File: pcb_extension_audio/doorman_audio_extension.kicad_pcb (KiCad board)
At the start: 4 copper layers, 31.4 x 29.6 mm, 45 parts, among them J1 Audio Out, J2 GPIO, J4 Extension Board Connector, J5 Audio In, U1 ES8388

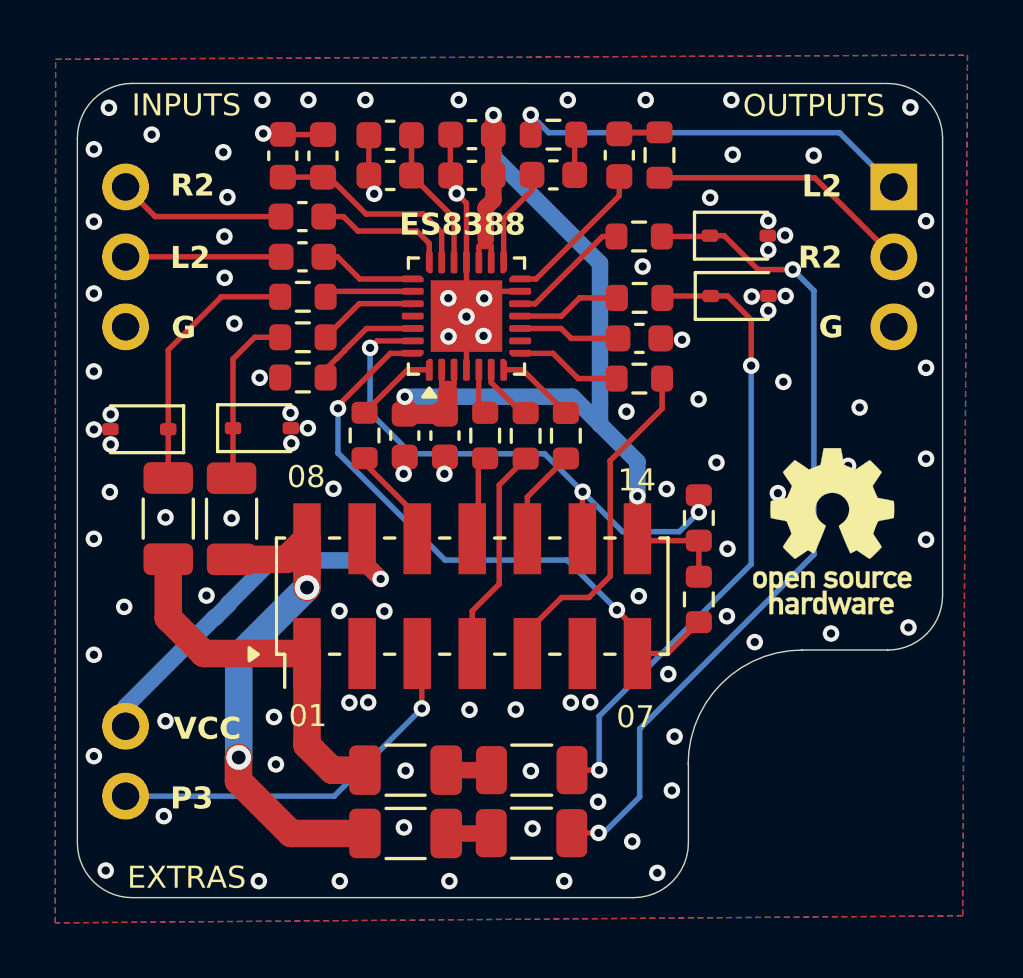
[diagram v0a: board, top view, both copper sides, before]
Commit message: WIP virtual devices
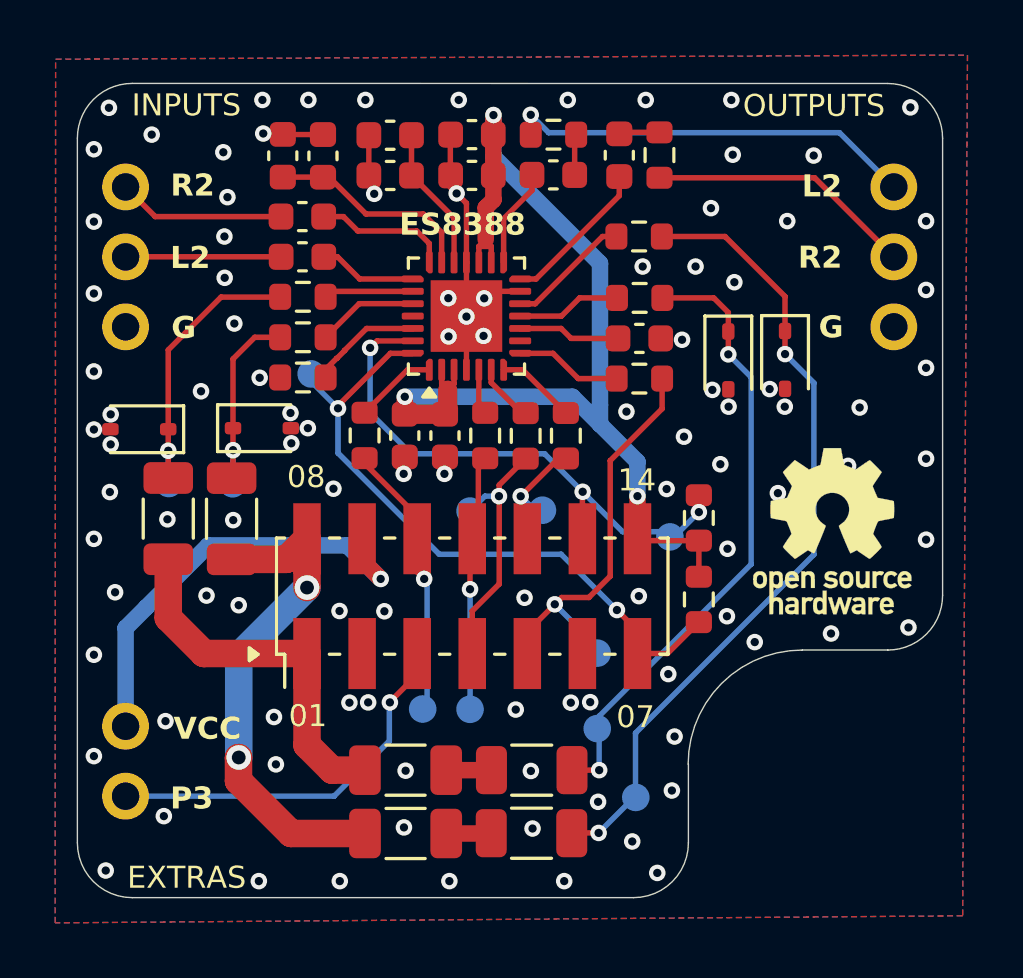
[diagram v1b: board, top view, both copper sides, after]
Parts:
- added TP1: Test Point IN L1, TestPoint:TestPoint_Pad_D1.0mm, B.Cu at (89.0, 62.4)
- added TP10: Test Point I2S DAT IN, TestPoint:TestPoint_Pad_D1.0mm, B.Cu at (97.6, 63.3)
- added TP11: Test Point I2S DAT OUT, TestPoint:TestPoint_Pad_D1.0mm, B.Cu at (102.2, 68.5)
- added TP2: Test Point IN R1, TestPoint:TestPoint_Pad_D1.0mm, B.Cu at (86.7, 62.3)
- added TP3: Test Point OUT L1, TestPoint:TestPoint_Pad_D1.0mm, B.Cu at (103.6, 73.7)
- added TP4: Test Point OUT R1, TestPoint:TestPoint_Pad_D1.0mm, B.Cu at (102.2, 71.2)
- added TP5: Test Point I2C CLK, TestPoint:TestPoint_Pad_D1.0mm, B.Cu at (91.8, 58.4)
- added TP6: Test Point I2C DAT, TestPoint:TestPoint_Pad_D1.0mm, B.Cu at (104.9, 64.3)
- added TP7: Test Point I2S MCLK, TestPoint:TestPoint_Pad_D1.0mm, B.Cu at (95.9, 70.5)
- added TP8: Test Point I2S BCLK, TestPoint:TestPoint_Pad_D1.0mm, B.Cu at (97.6, 70.5)
- added TP9: Test Point I2S LRCLK, TestPoint:TestPoint_Pad_D1.0mm, B.Cu at (100.2, 63.3)
- D1, D2, D3, D4: value CDSOD323-T03S -> TPCDSOD323-T03SC
- moved D2 4.81 mm to (109.0, 57.9), turned to -90 degrees
- moved D4 2.38 mm to (107.0, 57.9), turned to -90 degrees
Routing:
- net I2S_MCLK: track 4.13 -> 10.5 mm, vias 0 -> 1
- net I2S_BCLK: track 3.15 -> 9.38 mm, vias 0 -> 1
- net I2S_DAT_OUT: track 12.6 -> 15.0 mm, vias 0 -> 1
- net VCC: track 14.3 -> 16.4 mm
- net I2C_CLK: track 22.3 -> 24.0 mm
- net I2S_LRCK: track 3.49 -> 4.88 mm, vias 0 -> 1
- net I2S_DAT_IN: track 7.94 -> 9.22 mm, vias 0 -> 1
- net Net-(D1-K): track 6.39 -> 7.61 mm, vias 0 -> 1
- net Net-(D3-K): track 9.52 -> 10.7 mm, vias 0 -> 1
- net Net-(D2-K): track 30.4 -> 29.5 mm
- net PIN3: track 14.7 -> 14.0 mm
- net GND: vias 102 -> 104
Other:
- board text added: "08 BUS 09 VCC 10 I²S MCLK 11 I²S BCLK 12 I²S LRCK 13 I²C DAT 14 3V3"
- board text added: "BUS 01 GND 02 P3 03 I²S DIN 04 I²S DOUT 05 GND 06 I²C CLK 07"
- board text removed: "08 BUS 09 VCC 10 I²S BCLK 11 I²S DIN 12 I²S LRCK 13 I²C DAT 14 3V3"
- board text removed: "BUS 01 GND 02 I²S MCLK 03 P4 04 I²S DOUT 05 GND 06 I²C CLK 07"

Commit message: WIP
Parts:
- removed C13: 1uF, Capacitor_SMD:C_0603_1608Metric
- removed J5: Audio In, Connector_PinHeader_2.54mm:PinHeader_1x03_P2.54mm_Vertical
- removed R4, R7, R8, R9: 0, Resistor_SMD:R_0603_1608Metric
- removed U1: ES8388, Package_DFN_QFN:QFN-28-1EP_4x4mm_P0.45mm_EP2.6x2.6mm
- added C6: 1uF, Capacitor_SMD:C_0603_1608Metric, F.Cu at (89.3, 50.1)
- added J3: ~, Connector_PinHeader_2.54mm:PinHeader_1x03_P2.54mm_Vertical, F.Cu at (85.1, 55.7)
- added R1: 10K, Resistor_SMD:R_0603_1608Metric, F.Cu at (98.5, 49.3)
- added R11: 10K, Resistor_SMD:R_0603_1608Metric, F.Cu at (95.4, 50.8)
- added R12: 10K, Resistor_SMD:R_0603_1608Metric, F.Cu at (93.0, 52.3)
- added U2: ES8311, Doorman:QFN40P300X300X60-21N, F.Cu at (96.8, 55.6)
- J1: value Audio Out -> ~; moved to F.Cu
- R2, R3: value 10 -> 10K
- moved C5 17.6 mm to (108.6, 58.5), turned to 0 degrees
- moved C3 17.5 mm to (108.5, 56.6), turned to 0 degrees
- moved TP3 15.7 mm to (110.1, 59.5)
- moved TP7 14.4 mm to (91.7, 56.7)
- moved TP4 13.1 mm to (107.8, 59.4)
- moved C7 12.2 mm to (88.6, 53.1), turned to -90 degrees
- moved C20 11.9 mm to (102.7, 50.1)
- moved C2 11.2 mm to (100.3, 60.6), turned to 90 degrees
- moved C1 10.3 mm to (101.8, 60.6), turned to 90 degrees
- moved TP9 10.1 mm to (90.9, 59.4)
- moved R3 9.14 mm to (95.4, 49.4), turned to 0 degrees
- moved C21 9.03 mm to (101.3, 50.1)
- moved C19 8.36 mm to (102.0, 53.8), turned to 180 degrees
- moved R19 8.12 mm to (95.9, 60.6), turned to -90 degrees
- moved C18 7.39 mm to (102.0, 52.3), turned to 180 degrees
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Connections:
- net Net-(U1-ADCVREF) renamed ADCVREF
- net Net-(U1-VMID) renamed VMID
- C1 pad 2: +3.3V -> AVDD
- C10 pad 2: +3.3V -> AVDD
- C11 pad 2: +3.3V -> AVDD
- C12 pad 2: Net-(D3-K) -> AUDIO_IN_P
- C17 pad 2: Net-(U1-VREF) -> DACVREF
- C2 pad 2: +3.3V -> AVDD
- C3 pad 1: Net-(U1-RIN2) -> AUDIO_OUT_P
- C3 pad 2: AUDIO_IN_R2 -> Net-(J1-Pin_2)
- C4 pad 2: Net-(D1-K) -> AUDIO_IN_N
- C5 pad 1: Net-(U1-LIN2) -> AUDIO_OUT_N
- C5 pad 2: AUDIO_IN_L2 -> Net-(J1-Pin_1)
- C7 pad 1: Net-(U1-LOUT2) -> AUDIO_IN_N
- C7 pad 2: Net-(C7-Pad2) -> Net-(J3-Pin_1)
- D1 pad 1: Net-(D1-K) -> AUDIO_IN_N
- D2 pad 1: Net-(D2-K) -> AUDIO_OUT_P
- D3 pad 1: Net-(D3-K) -> AUDIO_IN_P
- D4 pad 1: Net-(D4-K) -> AUDIO_OUT_N
- J1 pad 1: AUDIO_OUT_L2 -> Net-(J1-Pin_1)
- J1 pad 2: AUDIO_OUT_R2 -> Net-(J1-Pin_2)
- J2 pad 1: PIN3 -> PIN2
- J2 pad 2: VCC -> GND
- J4 pad 11: I2S_BCLK -> I2S_LRCK
- J4 pad 12: I2S_LRCK -> I2S_DAT_IN
- J4 pad 14: +3.3V -> AVDD
- J4 pad 2: GND -> PIN2
- J4 pad 3: PIN3 -> GND
- J4 pad 4: I2S_DAT_IN -> I2S_BCLK
- J4 pad 9: VCC -> GND
- R10 pad 1: Net-(D2-K) -> AUDIO_OUT_P
- R13 pad 1: +3.3V -> AVDD
- R14 pad 1: +3.3V -> AVDD
- R2 pad 1: Net-(C7-Pad2) -> AUDIO_IN_N
- R2 pad 2: AUDIO_OUT_L2 -> GND
- R3 pad 1: Net-(C13-Pad2) -> AVDD
- R3 pad 2: AUDIO_OUT_R2 -> AUDIO_IN_P
- R5 pad 1: GND -> CE
- R5 pad 2: Net-(U1-CE) -> GND
- R6 pad 1: Net-(D4-K) -> AUDIO_OUT_N
- TP1 pad 1: Net-(D1-K) -> AUDIO_IN_N
- TP2 pad 1: Net-(D3-K) -> AUDIO_IN_P
- TP3 pad 1: Net-(D2-K) -> AUDIO_OUT_P
- TP4 pad 1: Net-(D4-K) -> AUDIO_OUT_N
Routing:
- net AVDD: track 0.00 -> 55.8 mm, vias 0 -> 5
- net +3.3V: track 40.3 -> 0.00 mm, vias 3 -> 0
- net AUDIO_OUT_P: track 0.00 -> 34.7 mm, vias 0 -> 2
- net Net-(D2-K): track 29.5 -> 0.00 mm, vias 2 -> 0
- net AUDIO_OUT_N: track 0.00 -> 29.2 mm, vias 0 -> 2
- net AUDIO_IN_P: track 0.00 -> 27.6 mm, vias 0 -> 3
- net AUDIO_IN_N: track 0.00 -> 26.8 mm, vias 0 -> 3
- net Net-(D4-K): track 22.9 -> 0.00 mm, vias 2 -> 0
- net PIN2: track 0.00 -> 17.0 mm, vias 0 -> 1
- net VCC: track 16.4 -> 0.00 mm, vias 1 -> 0
- net AUDIO_OUT_L2: track 15.0 -> 0.00 mm, vias 1 -> 0
- net PIN3: track 14.0 -> 0.00 mm, vias 1 -> 0
- net Net-(D3-K): track 10.7 -> 0.00 mm, vias 1 -> 0
- net AUDIO_OUT_R2: track 9.70 -> 0.00 mm
- net GND: track 14.0 -> 5.14 mm, vias 104 -> 92
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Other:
- board text added: "+"
- board text added: "-"
- board text added: "08 BUS 09 GND 10 I²S MCLK 11 I²S LRCK 12 I²S DIN 13 I²C DAT 14 3V3"
- board text added: "BUS 01 P2 02 GND 03 I²S BCLK 04 I²S DOUT 05 GND 06 I²C CLK 07"
- board text added: "ES8311"
- board text added: "GND"
- board text added: "GPIO"
- board text added: "INPUT"
- board text added: "OUTPUT"
- board text added: "P2"
- board text removed: "08 BUS 09 VCC 10 I²S MCLK 11 I²S BCLK 12 I²S LRCK 13 I²C DAT 14 3V3"
- board text removed: "BUS 01 GND 02 P3 03 I²S DIN 04 I²S DOUT 05 GND 06 I²C CLK 07"
- board text removed: "ES8388"
- board text removed: "EXTRAS"
- board text removed: "INPUTS"
- board text removed: "L2"
- board text removed: "OUTPUTS"
- board text removed: "P3"
- board text removed: "R2"
- board text removed: "VCC"

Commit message: WIP
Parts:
- added C13: 10uF, Capacitor_SMD:C_0402_1005Metric, F.Cu at (96.0, 51.8)
- added C9: 10uF, Capacitor_SMD:C_0402_1005Metric, F.Cu at (97.8, 51.8)
- J1: value ~ -> Output
- J3: value ~ -> Input
- moved TP5 16.6 mm to (104.7, 65.6)
- moved J1 2.93 mm to (113.0, 55.7)
- moved TP7 2.28 mm to (91.5, 54.5)
- moved C7 1.85 mm to (88.4, 54.9)
- moved C5 0.26 mm to (108.3, 58.4)
- moved C3 0.22 mm to (108.3, 56.6)
- moved R1 0.19 mm to (98.4, 49.2)
- moved R2 0.19 mm to (98.4, 50.6)
- moved R3 0.19 mm to (95.5, 49.2)
- moved R11 0.19 mm to (95.5, 50.6)
- moved C6 0.09 mm to (89.2, 50.1)
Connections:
- C12 pad 2: AUDIO_IN_P -> Net-(D3-K)
- C4 pad 2: AUDIO_IN_N -> Net-(D1-K)
- D1 pad 1: AUDIO_IN_N -> Net-(D1-K)
- D3 pad 1: AUDIO_IN_P -> Net-(D3-K)
- R1 pad 1: AVDD -> Net-(D1-K)
- R1 pad 2: AUDIO_IN_N -> Net-(C9-Pad2)
- R11 pad 1: AUDIO_IN_P -> Net-(C13-Pad2)
- R2 pad 1: AUDIO_IN_N -> Net-(C9-Pad2)
- R3 pad 1: AVDD -> Net-(D3-K)
- R3 pad 2: AUDIO_IN_P -> Net-(C13-Pad2)
- TP1 pad 1: AUDIO_IN_N -> Net-(D1-K)
- TP2 pad 1: AUDIO_IN_P -> Net-(D3-K)
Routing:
- net Net-(D1-K): track 0.00 -> 23.5 mm, vias 0 -> 2
- net Net-(D3-K): track 0.00 -> 20.9 mm, vias 0 -> 2
- net AUDIO_IN_P: track 27.6 -> 9.62 mm, vias 3 -> 0
- net AVDD: track 55.8 -> 37.9 mm, vias 5 -> 4
- net AUDIO_IN_N: track 26.8 -> 15.5 mm, vias 3 -> 2
- net I2C_DAT: track 22.6 -> 26.8 mm
- net Net-(C13-Pad2): track 0.00 -> 2.81 mm
- net Net-(C9-Pad2): track 0.00 -> 2.77 mm
- net I2C_CLK: track 25.8 -> 24.3 mm
- net Net-(J1-Pin_1): track 4.04 -> 5.22 mm
- net Net-(J1-Pin_2): track 4.24 -> 5.34 mm
- net Net-(J3-Pin_1): track 4.25 -> 3.29 mm
- net GND: vias 92 -> 96

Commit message: WIP
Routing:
- net GND: vias 96 -> 98
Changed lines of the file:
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@@
+	)
+	(via
+		(at 91.56 50.76)
+		(size 0.6)
+		(drill 0.3)
+		(layers "F.Cu" "B.Cu")
+		(free yes)
+		(net 1)
 	)
 	(via
@@
 		(size 0.6)
 		(drill 0.3)
+		(layers "F.Cu" "B.Cu")
+		(free yes)
+		(net 1)
+	)
+	(via
+		(at 101.92 66.31)
+		(size 0.6)
+		(drill 0.3)

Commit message: Core Board V2.0.0
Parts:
- moved C14 0.80 mm to (96.0, 72.4)
- moved R6 0.80 mm to (100.6, 72.4)
- moved R10 0.72 mm to (100.6, 75.0)
- moved C8 0.72 mm to (96.0, 75.0)
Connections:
- C14 pad 1: BUS_WIRE2 -> BUS_WIRE1
- C8 pad 1: BUS_WIRE1 -> BUS_WIRE2
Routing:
- net BUS_WIRE2: track 14.3 -> 17.0 mm
- net BUS_WIRE1: track 16.1 -> 14.3 mm
- net AUDIO_OUT_N: track 28.9 -> 28.3 mm
- net I2C_DAT: track 26.8 -> 26.2 mm
- net AVDD: vias 4 -> 3
